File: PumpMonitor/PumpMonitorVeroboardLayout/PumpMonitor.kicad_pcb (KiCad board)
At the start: 2 copper layers, 119.4 x 55.9 mm, 29 parts, among them J1 Power & Current Sense, J2 Programming, J3 Ra01_Breakout_Module, Q1 BC548, Q2 BC548, SW1 SW_Push, U1 LM317_TO-220, U2 24LC16, U3 PICAXE-18M2

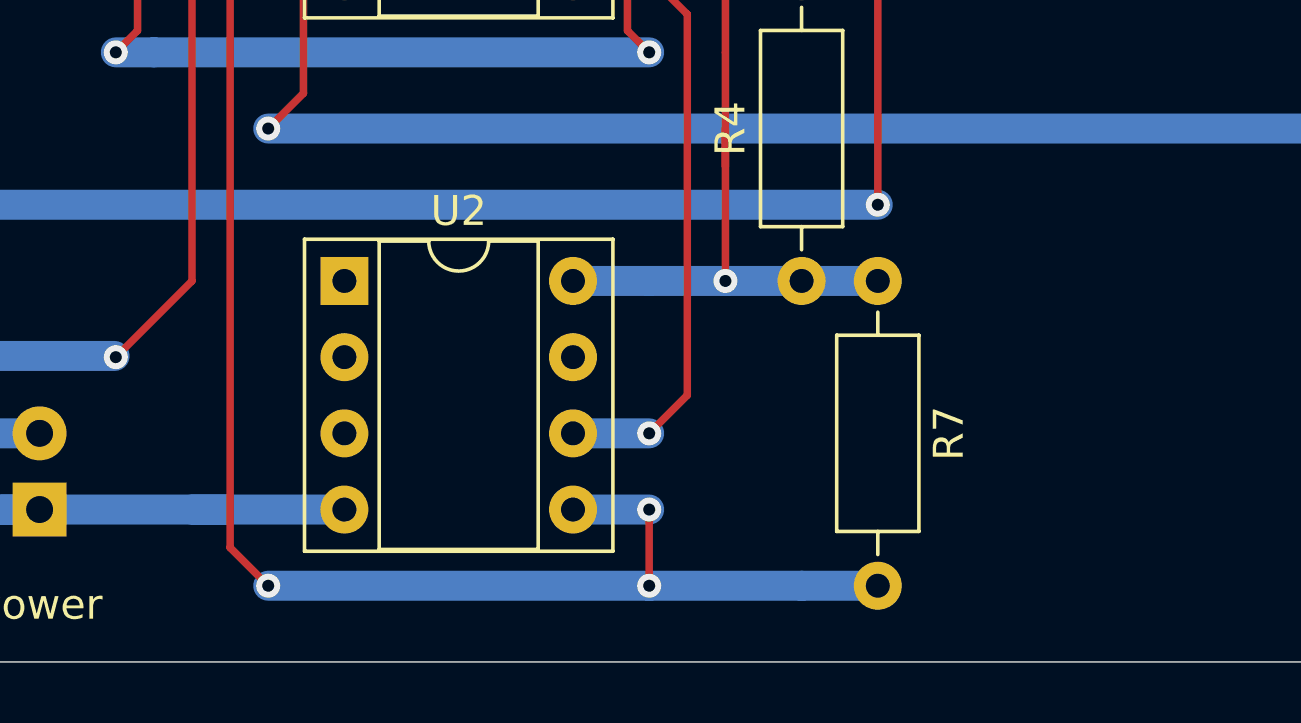
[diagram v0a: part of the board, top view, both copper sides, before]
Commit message: Added temperature sensor CRC check
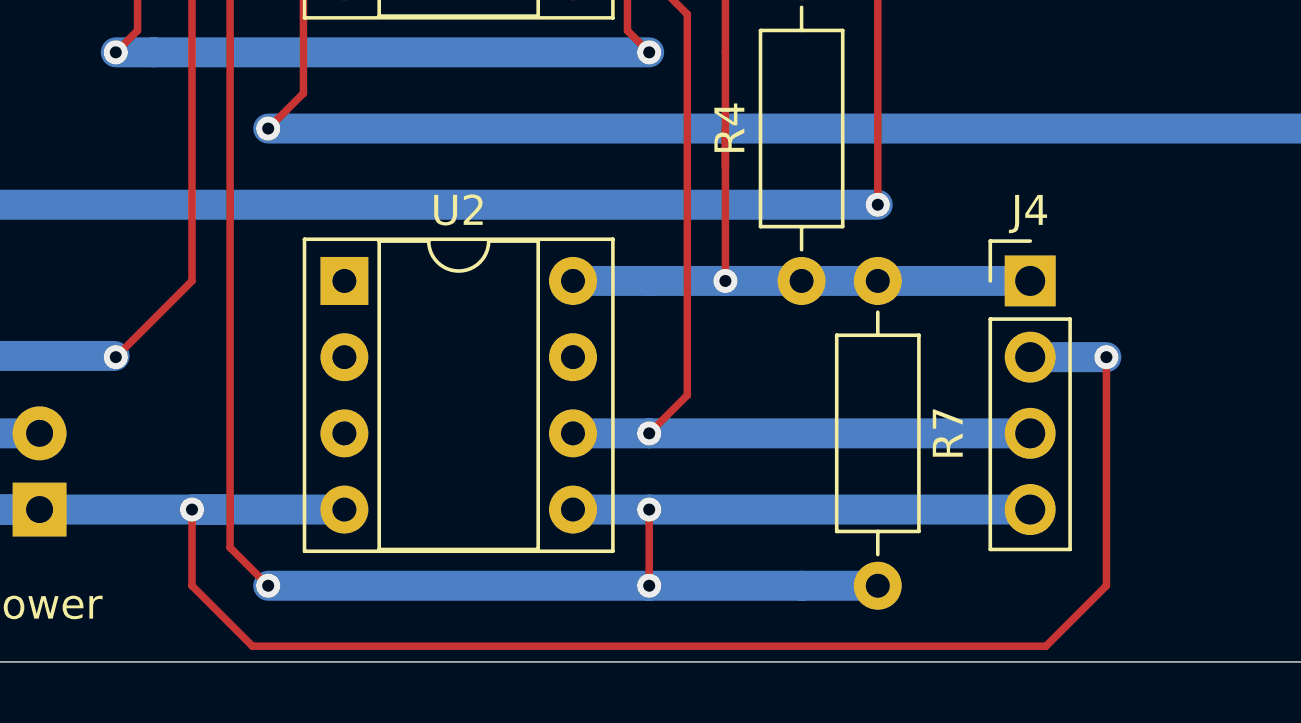
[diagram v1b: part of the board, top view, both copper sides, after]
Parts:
- added J4: AHT20 Temperature Sensor, Connector_PinHeader_2.54mm:PinHeader_1x04_P2.54mm_Vertical, F.Cu at (195.6, 139.7)
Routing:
- net Earth: track 259.8 -> 304.6 mm, vias 15 -> 17
- net Net-(J4-Pin_4): track 54.4 -> 67.1 mm
- net Net-(J4-Pin_3): track 26.5 -> 39.2 mm
- net +3V3: track 256.6 -> 261.7 mm
